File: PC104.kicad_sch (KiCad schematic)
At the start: 2 parts

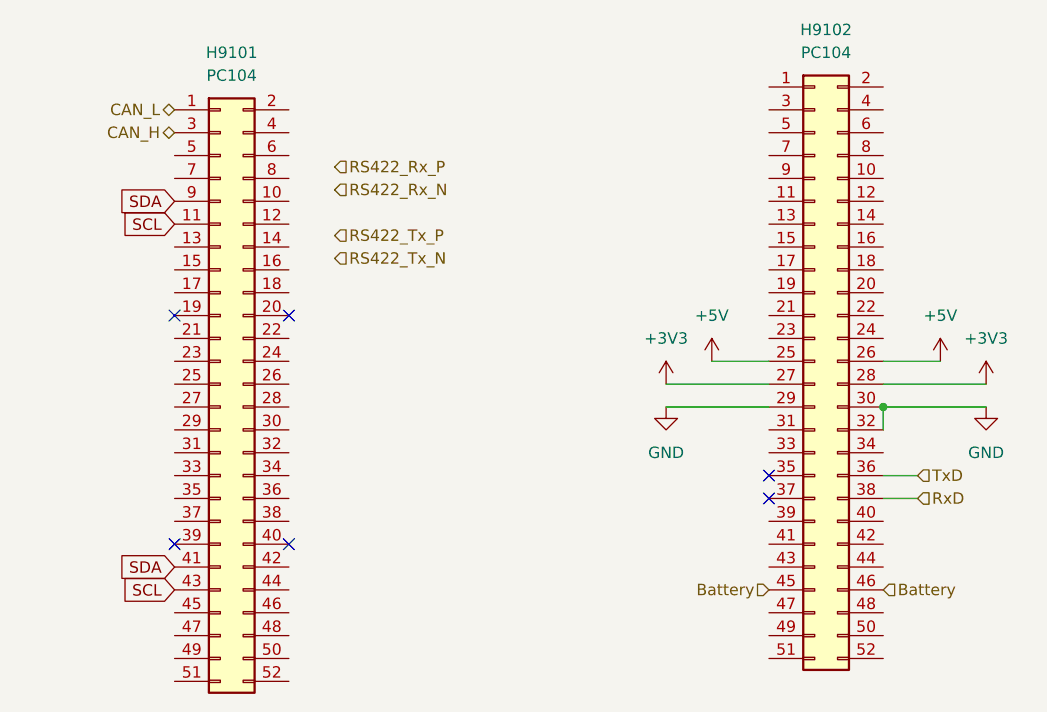
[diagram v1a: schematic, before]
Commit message: restructurization of the entire project improved
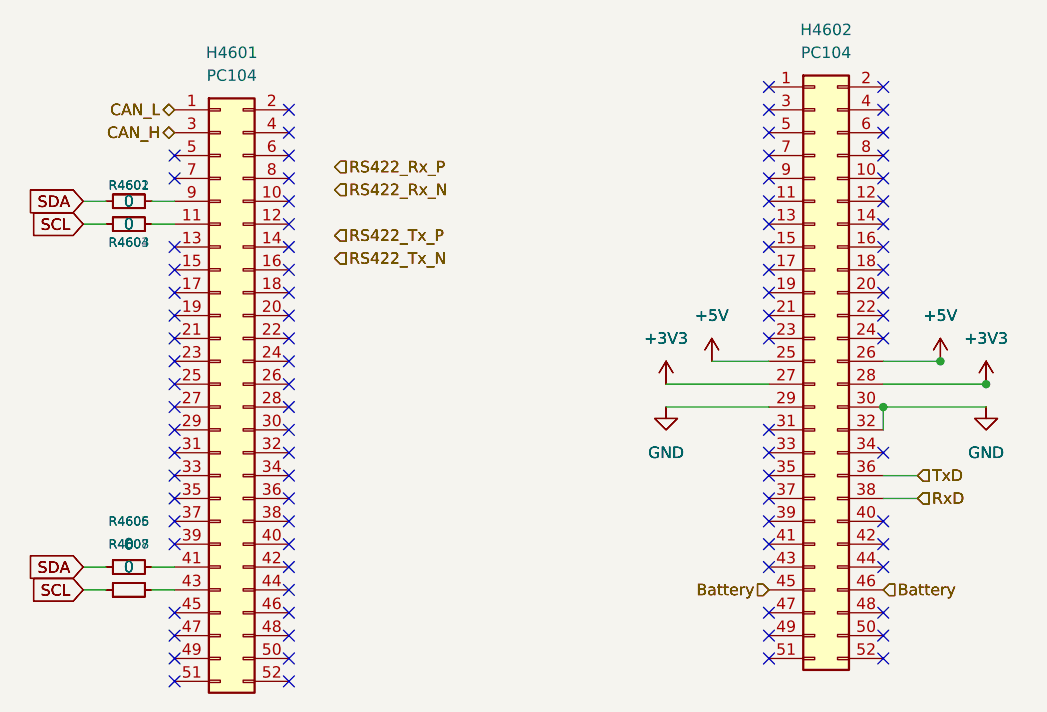
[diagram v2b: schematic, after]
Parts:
- removed H9101: PC104, Connector_PinSocket_2.54mm:PinSocket_2x26_P2.54mm_Vertical, symbol Connector_Generic:Conn_02x26_Odd_Even
- added H4601: PC104, Connector_PinSocket_2.54mm:PinSocket_2x26_P2.54mm_Vertical, symbol Connector_Generic:Conn_02x26_Odd_Even
- added R4601, R4602, R4603, R4604, R4605, R4606, R4607, R4608: 0, Resistor_SMD:R_0603_1608Metric_Pad0.98x0.95mm_HandSolder, symbol Device:R_Small
- renumbered H9102 to H4602
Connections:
- net CAN_H: now also H4601.3 (Pin_3)
- net CAN_L: now also H4601.1 (Pin_1)
- net SCL: now also R4603.1, R4604.1, R4607.1, R4608.1
- net SDA: now also R4601.1, R4602.1, R4605.1, R4606.1
- new net: H4601.9 (Pin_9), R4601.2, R4602.2
- new net: H4601.41 (Pin_41), R4605.2, R4606.2
- new net: H4601.11 (Pin_11), R4603.2, R4604.2
- new net: H4601.43 (Pin_43), R4607.2, R4608.2
- no-connect marks 6 -> 87

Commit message: progress on CORE pcb
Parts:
- removed R4602, R4604, R4605, R4607: 0, Resistor_SMD:R_0603_1608Metric_Pad0.98x0.95mm_HandSolder, symbol Device:R_Small
- added R1202, R1204: 0, Resistor_SMD:R_0603_1608Metric_Pad0.98x0.95mm_HandSolder, symbol Device:R_Small
- renumbered H4602 to H1201, H4601 to H1202, R4601 to R1201, R4603 to R1203, R4606 to R1206, R4608 to R1208
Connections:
- net RxD: now also R1204.2; no longer H1201.38 (Pin_38)
- net TxD: now also R1202.2; no longer H1201.36 (Pin_36)
- new net: H1201.38 (Pin_38), R1204.1
- new net: H1201.36 (Pin_36), R1202.1

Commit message: nearly finnished CORE pcb
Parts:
- added R1205, R1207, R1209, R1210: 0, Resistor_SMD:R_0603_1608Metric_Pad0.98x0.95mm_HandSolder, symbol Device:R_Small
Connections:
- net +3V3: now also R1205.2, R1207.1; no longer H1201.27 (Pin_27), H1201.28 (Pin_28)
- net +5V: now also R1209.1, R1210.2; no longer H1201.25 (Pin_25), H1201.26 (Pin_26)
- new net: H1201.26 (Pin_26), R1210.1
- new net: H1201.25 (Pin_25), R1209.2
- new net: H1201.27 (Pin_27), R1207.2
- new net: H1201.28 (Pin_28), R1205.1

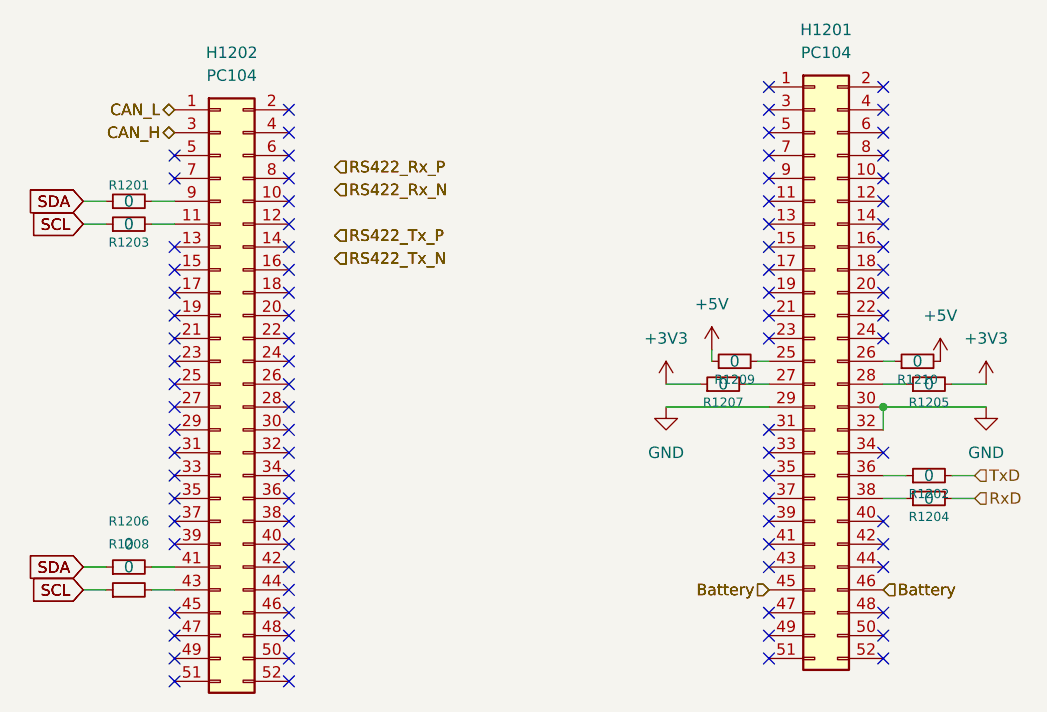
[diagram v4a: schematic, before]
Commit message: pcb progres for all components
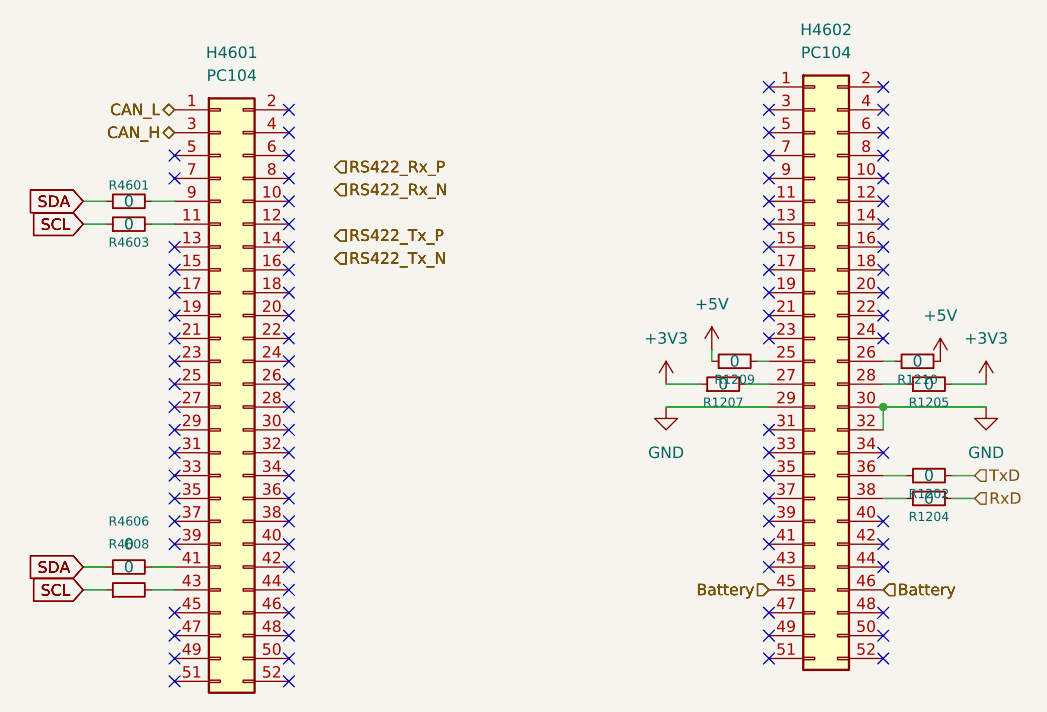
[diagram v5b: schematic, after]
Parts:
- renumbered H1202 to H4601, H1201 to H4602, R1201 to R4601, R1203 to R4603, R1206 to R4606, R1208 to R4608

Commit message: progress on PCBs
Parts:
- renumbered H4602 to H1901, H4601 to H1902, R4601 to R1901, R4603 to R1902, R1209 to R1903, R1210 to R1904, R1207 to R1905, R1205 to R1906, R1202 to R1907, R1204 to R1908, R4606 to R1909, R4608 to R1910
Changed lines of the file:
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@@
 		(on_board yes)
 		(dnp no)
-		(property "Reference" "R4601"
+		(property "Reference" "R1901"
 			(at 83.82 45.212 90)
 			(effects
@@
 		(dnp no)
 		(fields_autoplaced yes)
-		(property "Reference" "#PWR04601"
+		(property "Reference" "#PWR01903"
 			(at 143.51 71.12 0)
 			(effects
@@
 		(dnp no)
 		(fields_autoplaced yes)
-		(property "Reference" "H4601"
+		(property "Reference" "H1902"
 			(at 95.25 30.48 0)
 			(effects
@@
 		(dnp no)
 		(fields_autoplaced yes)
-		(property "Reference" "R4606"
+		(property "Reference" "R1909"
 			(at 83.82 82.55 90)
 			(effects
@@
 		(on_board yes)
 		(dnp no)
-		(property "Reference" "R4603"
+		(property "Reference" "R1902"
 			(at 83.82 51.562 90)
 			(effects
@@
 		(dnp no)
 		(fields_autoplaced yes)
-		(property "Reference" "#PWR04612"
+		(property "Reference" "#PWR01906"
 			(at 179.07 76.2 0)
 			(effects
@@
 		(dnp no)
 		(fields_autoplaced yes)
-		(property "Reference" "#PWR04605"
+		(property "Reference" "#PWR01901"
 			(at 148.59 67.31 0)
 			(effects
@@
 		(dnp no)
 		(fields_autoplaced yes)
-		(property "Reference" "#PWR04608"
+		(property "Reference" "#PWR01902"
 			(at 173.99 68.58 0)
 			(effects
@@
 		(on_board yes)
 		(dnp no)
-		(property "Reference" "R?"
+		(property "Reference" "R1908"
 			(at 172.72 82.042 90)
 			(effects
@@
 		(on_board yes)
 		(dnp no)
-		(property "Reference" "R?"
+		(property "Reference" "R1904"
 			(at 171.45 66.802 90)
 			(effects
@@
 		(dnp no)
 		(fields_autoplaced yes)
-		(property "Reference" "#PWR04610"
+		(property "Reference" "#PWR01904"
 			(at 179.07 71.12 0)
 			(effects
@@
 		(on_board yes)
 		(dnp no)
-		(property "Reference" "R?"
+		(property "Reference" "R1907"
 			(at 172.72 79.502 90)
 			(effects
@@
 		(dnp no)
 		(fields_autoplaced yes)
-		(property "Reference" "R4608"
+		(property "Reference" "R1910"
 			(at 83.82 85.09 90)
 			(effects
@@
 		(dnp no)
 		(fields_autoplaced yes)
-		(property "Reference" "H4602"
+		(property "Reference" "H1901"
 			(at 161.29 27.94 0)
 			(effects
@@
 		(dnp no)
 		(fields_autoplaced yes)
-		(property "Reference" "#PWR04604"
+		(property "Reference" "#PWR01905"
 			(at 143.51 76.2 0)
 			(effects
@@
 		(on_board yes)
 		(dnp no)
-		(property "Reference" "R?"
+		(property "Reference" "R1903"
 			(at 151.13 66.802 90)
 			(effects
@@
 		(on_board yes)
 		(dnp no)
-		(property "Reference" "R?"
+		(property "Reference" "R1906"
 			(at 172.72 69.342 90)
 			(effects
@@
 		(on_board yes)
 		(dnp no)
-		(property "Reference" "R?"
+		(property "Reference" "R1905"
 			(at 149.86 69.342 90)
 			(effects
